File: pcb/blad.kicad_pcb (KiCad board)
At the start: 2 copper layers, 228.6 x 76.2 mm, 95 parts, among them J1 Conn_01x04, J2 Conn_01x02_Pin, SW1 1U, SW10 1U, SW11 1U, SW12 1U, SW13 1.25U, SW14 1U, SW15 1U, SW16 1U, SW17 1U, SW18 1U, SW19 1U, SW2 1U, SW20 1U, SW21 1U, SW22 1U, SW23 1.75U, SW24 1U, SW25 1U, SW26 1U, SW27 1U, SW28 1U, SW29 1U, SW3 1U, SW30 1U, SW31 1U, SW32 1U, SW33 1.25U, SW34 1.25U, SW35 1U, SW36 1.25U, SW37 2.75U, SW38 1.25U, SW39 1U, SW4 1U, SW40 1.25U, SW41 1.75U, SW42 2.25U, SW5 1U, SW6 1U, SW7 1U, SW8 1U, SW9 1U, U1 HY0020

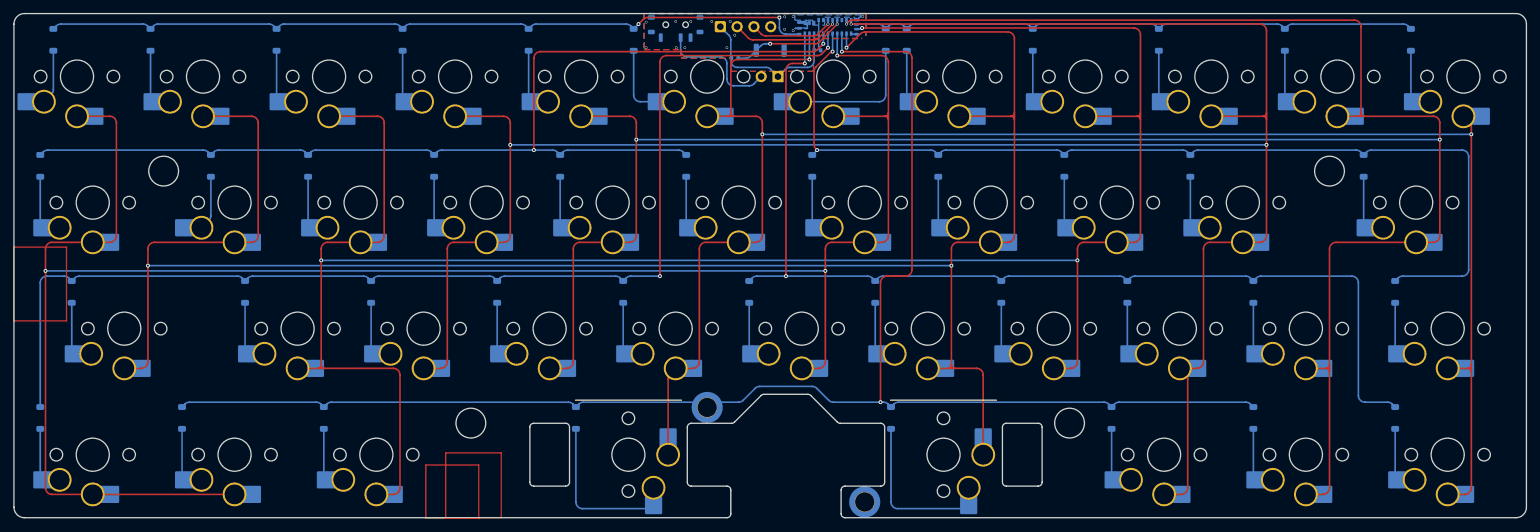
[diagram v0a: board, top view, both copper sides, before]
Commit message: Migrate PCB to MS88SF21 module
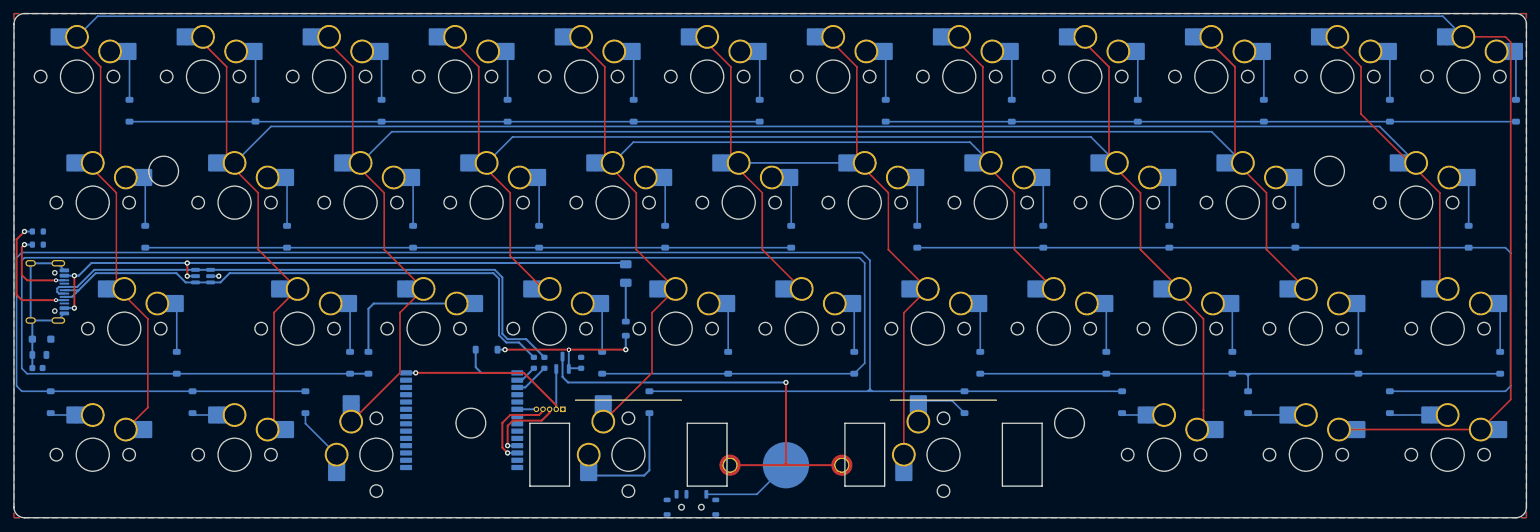
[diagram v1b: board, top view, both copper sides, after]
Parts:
- removed H1 (x2): MountingHole, Smidr:SMD-1_BD4.4-D2.8
- removed the SW25 at (151.6, 157.2)
- removed TS1: RST, Button_Switch_SMD:SW_Push_SPST_NO_Alps_SKRK
- added BT1: Battery_Cell, Smidr:BatteryHolder_Takachi_BS-S-1632, B.Cu at (206.4, 177.8)
- added D43: 1N5819W, Diode_SMD:D_SOD-123, B.Cu at (161.1, 160.3)
- added D44: SMF5.0CA, Diode_SMD:D_SOD-123F, B.Cu at (93.9, 158.8)
- added F1: PTC 500mA Hold, Fuse:Fuse_1206_3216Metric, B.Cu at (182.2, 148.8)
- added L1: BLM21PG121SN1D, Inductor_SMD:L_0805_2012Metric, B.Cu at (182.2, 157.2)
- added L2: BLM21PG121SN1D, Inductor_SMD:L_0805_2012Metric, B.Cu at (93.5, 161.1)
- added Q1: AO3401A, Package_TO_SOT_SMD:SOT-23, B.Cu at (172.6, 162.3)
- added R2: 100k, Resistor_SMD:R_0603_1608Metric, B.Cu at (175.4, 162.3)
- added R3: 5.1k, Resistor_SMD:R_0603_1608Metric, B.Cu at (93.3, 144.5)
- added R4: 27, Resistor_SMD:R_0603_1608Metric, B.Cu at (168.3, 162.3)
- added R5: 27, Resistor_SMD:R_0603_1608Metric, B.Cu at (169.9, 162.3)
- added SW26: 1U, Smidr:SW_Smidr_Choc_Hotswap, B.Cu at (151.6, 157.2)
- added U2: MS88SF21 1Y40AI-U, Smidr:RF_Module_MinewSemi_MS88SF21, B.Cu at (157.4, 174.1)
- C1: value 100nF -> 100n; footprint Capacitor_SMD:C_0402_1005Metric -> Capacitor_SMD:C_0603_1608Metric
- J1: value Conn_01x04 -> HRO_TYPE-C-31-M-12; footprint Connector_PinHeader_2.54mm:PinHeader_1x04_P2.54mm_Vertical -> Connector_USB:USB_C_Receptacle_HRO_TYPE-C-31-M-12
- J2: value Conn_01x02_Pin -> SWD; footprint Connector_PinHeader_2.54mm:PinHeader_1x02_P2.54mm_Vertical -> Connector_PinHeader_1.00mm:PinHeader_1x05_P1.00mm_Vertical
- R1: value 10k -> 5.1k; footprint Resistor_SMD:R_0402_1005Metric -> Resistor_SMD:R_0603_1608Metric
- U1: value HY0020 -> SRV05-4; footprint Smidr:RF_Module_FDK_HY0020 -> Package_TO_SOT_SMD:SOT-23-6
- moved C1 127.3 mm to (93.2, 163.1)
- moved J1 110.7 mm to (93.3, 151.6), turned to 90 degrees
- moved R1 108.5 mm to (93.3, 142.5)
- moved U1 101.7 mm to (118.3, 149.2), turned to 180 degrees
- moved S1 73.0 mm to (192.1, 184.2), turned to 180 degrees
- moved J2 59.9 mm to (172.7, 169.3)
- moved D6 21.9 mm to (202.4, 124.2), turned to 90 degrees
- moved D5 19.2 mm to (183.4, 124.2), turned to 90 degrees
- moved D8 19.2 mm to (240.5, 124.2), turned to 90 degrees
- moved D24 19.2 mm to (114.3, 162.3), turned to 90 degrees
- moved D34 19.2 mm to (314.3, 162.3), turned to 90 degrees
- moved D15 19.2 mm to (150.0, 143.3), turned to 90 degrees
- moved D20 19.2 mm to (245.3, 143.3), turned to 90 degrees
- moved D21 19.2 mm to (264.3, 143.3), turned to 90 degrees
- moved D28 19.2 mm to (197.6, 162.3), turned to 90 degrees
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- renumbered D41 to D24, D24 to D25, D25 to D26, D26 to D27, D27 to D28, D28 to D29, D29 to D30, D30 to D31, D31 to D32, D32 to D33, D33 to D34, D34 to D35, D35 to D36, D36 to D37, D37 to D38, D42 to D39, D38 to D40, D39 to D41, D40 to D42, SW41 to SW24, SW24 to SW25, SW26 to SW27, SW27 to SW28, SW28 to SW29, SW29 to SW30, SW30 to SW31, SW31 to SW32, SW32 to SW33, SW33 to SW34, SW34 to SW35, SW35 to SW36, SW36 to SW37, SW37 to SW38, SW42 to SW39, SW38 to SW40, SW39 to SW41, SW40 to SW42
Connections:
- C1 pad 1: +3V0 -> Earth
- D29 pad 1: ROW5 -> ROW4
- D34 pad 1: ROW3 -> ROW5
- D35 pad 1: ROW4 -> ROW6
- D35 pad 2: Net-(D34-A) (its old number) -> Net-(D35-A)
- D36 pad 2: Net-(D35-A) -> Net-(D36-A)
- D37 pad 2: Net-(D36-A) -> Net-(D37-A)
- D38 pad 2: Net-(D37-A) -> Net-(D38-A)
- D40 pad 2: Net-(D38-A) -> Net-(D40-A)
- D41 pad 1: ROW6 -> ROW5
- D41 pad 2: Net-(D39-A) (its old number) -> Net-(D41-A)
- D42 pad 1: ROW5 -> ROW3
- D42 pad 2: Net-(D40-A) -> Net-(D42-A)
- J2 pad 1: +3V0 -> GND
- J2 pad 2: Net-(J2-Pin_2) -> VDD
- R1 pad 1: +3V0 -> Net-(J1-CC1)
- R1 pad 2: nRESET -> GND
- S1 pad 1: unconnected-(S1-A-Pad1) -> Net-(BT1--)
- S1 pad 2: Net-(J2-Pin_2) -> GND
- S1 pad 3: GND -> unconnected-(S1-C-Pad3)
- SW10 pad 2: COL3 -> COL2
- SW11 pad 2: COL4 -> COL1
- SW12 pad 2: COL5 -> COL0
- SW19 pad 2: COL0 -> COL5
- SW20 pad 2: COL1 -> COL4
- SW21 pad 2: COL2 -> COL3
- SW22 pad 2: COL3 -> COL2
- SW23 pad 2: COL4 -> COL1
- SW24 pad 2: COL1 -> COL0
- SW25 pad 2: COL2 -> COL1
- SW27 pad 2: COL4 -> COL3
- SW28 pad 2: COL5 -> COL4
- SW29 pad 2: COL0 -> COL5
- SW30 pad 2: COL1 -> COL5
- SW31 pad 2: COL2 -> COL4
- SW33 pad 2: COL4 -> COL2
- SW34 pad 2: COL5 -> COL1
- SW35 pad 1: Net-(D34-A) (its old number) -> COL0
- SW35 pad 2: COL0 -> Net-(D35-A)
- SW36 pad 1: Net-(D35-A) -> COL1
- SW36 pad 2: COL0 -> Net-(D36-A)
- SW37 pad 1: Net-(D36-A) -> COL2
- SW37 pad 2: COL2 -> Net-(D37-A)
- SW38 pad 1: Net-(D37-A) -> COL4
- SW38 pad 2: COL5 -> Net-(D38-A)
- SW39 pad 2: COL1 -> COL5
- SW40 pad 1: Net-(D38-A) -> COL3
- SW40 pad 2: COL3 -> Net-(D40-A)
- SW41 pad 1: Net-(D39-A) (its old number) -> COL0
- SW41 pad 2: COL4 -> Net-(D41-A)
- SW42 pad 1: Net-(D40-A) -> COL0
- SW42 pad 2: COL5 -> Net-(D42-A)
- SW7 pad 2: COL0 -> COL5
- SW8 pad 2: COL1 -> COL4
- SW9 pad 2: COL2 -> COL3
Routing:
- net COL4: track 369.4 -> 172.0 mm, vias 3 -> 0
- net COL5: track 269.5 -> 133.3 mm, vias 3 -> 0
- net COL3: track 331.1 -> 209.8 mm, vias 3 -> 0
- net VBUS: track 0.00 -> 95.4 mm, vias 0 -> 4
- net USB_D+: track 0.00 -> 87.0 mm
- net USB_D-: track 0.00 -> 86.0 mm
- net ROW4: track 176.2 -> 252.4 mm, vias 2 -> 0
- net ROW5: track 157.3 -> 82.5 mm, vias 2 -> 0
- net COL2: track 323.0 -> 249.5 mm, vias 3 -> 0
- net COL0: track 297.8 -> 367.6 mm, vias 3 -> 0
- net +BATT: track 0.00 -> 67.7 mm, vias 0 -> 1
- net ROW2: track 160.0 -> 97.6 mm, vias 2 -> 0
- net ROW6: track 235.9 -> 285.7 mm, vias 2 -> 0
- net VDD: track 0.00 -> 31.4 mm, vias 0 -> 1
- net Earth: track 0.00 -> 27.2 mm
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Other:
- outline, holes or cut-outs redrawn

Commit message: Update PCB power wiring and stabilizer cutouts
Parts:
- moved L1 18.9 mm to (163.5, 154.4)
- moved F1 18.7 mm to (163.5, 148.8)
- moved D43 9.73 mm to (170.7, 162.3)
- moved R5 8.92 mm to (161.5, 159.1)
- moved R4 8.92 mm to (159.9, 159.1)
- moved Q1 4.27 mm to (170.6, 166.1), turned to 180 degrees
- moved D42 2.38 mm to (300.0, 168.3)
- moved D41 2.38 mm to (278.6, 168.3)
- moved R2 0.89 mm to (175.8, 163.1), turned to 90 degrees
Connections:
- SW39 pad 1: Net-(D39-A) -> COL5
- SW39 pad 2: COL5 -> Net-(D39-A)
- U2 pad 10: unconnected-(U2-P0.08-Pad10) -> ROW2
- U2 pad 11: unconnected-(U2-P1.09-Pad11) -> ROW5
- U2 pad 12: unconnected-(U2-P0.12-Pad12) -> COL3
- U2 pad 18: unconnected-(U2-P0.13-Pad18) -> ROW1
- U2 pad 19: unconnected-(U2-P0.15-Pad19) -> ROW3
- U2 pad 2: unconnected-(U2-P1.13-Pad2) -> COL0
- U2 pad 21: unconnected-(U2-P0.20-Pad21) -> COL4
- U2 pad 22: unconnected-(U2-P0.22-Pad22) -> COL5
- U2 pad 5: unconnected-(U2-P0.29-Pad5) -> COL1
- U2 pad 6: unconnected-(U2-P0.31-Pad6) -> COL2
- U2 pad 7: unconnected-(U2-P0.26-Pad7) -> ROW6
- U2 pad 8: unconnected-(U2-P0.04-Pad8) -> ROW4
- U2 pad 9: unconnected-(U2-P0.06-Pad9) -> ROW0
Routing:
- net ROW1: track 95.2 -> 289.9 mm, vias 0 -> 2
- net ROW3: track 128.7 -> 263.9 mm, vias 0 -> 2
- net ROW5: track 82.5 -> 171.9 mm, vias 0 -> 2
- net COL5: track 133.3 -> 213.9 mm, vias 0 -> 1
- net COL0: track 367.6 -> 422.6 mm
- net ROW0: track 95.2 -> 143.6 mm, vias 0 -> 2
- net COL3: track 209.8 -> 248.4 mm, vias 0 -> 1
- net COL1: track 295.9 -> 332.4 mm
- net ROW2: track 97.6 -> 123.5 mm, vias 0 -> 2
- net VBUS: track 95.4 -> 76.7 mm
- net ROW6: track 285.7 -> 302.3 mm, vias 0 -> 2
- net COL4: track 172.0 -> 185.3 mm
- net ROW4: track 252.4 -> 263.2 mm, vias 0 -> 2
- net Net-(D39-A): track 7.74 -> 18.2 mm
- net USB_D+: track 87.0 -> 77.5 mm
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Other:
- outline, holes or cut-outs redrawn

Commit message: Add logo footprint to PCB
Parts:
- added G***: LOGO, Smidr:logo, F.Cu at (204.0, 147.6)
- moved U1 3.57 mm to (121.8, 149.2)
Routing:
- net ROW4: track 263.2 -> 223.0 mm, vias 2 -> 0
- net ROW6: track 302.3 -> 269.0 mm
- net GND: vias 1677 -> 1661
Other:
- outline, holes or cut-outs redrawn

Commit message: Fix USB grounding and add battery bulk capacitor
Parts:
- removed D44: SMF5.0CA, Diode_SMD:D_SOD-123F
- C1: value 100n -> 100u; footprint Capacitor_SMD:C_0603_1608Metric -> Capacitor_SMD:C_1206_3216Metric
- moved C1 96.6 mm to (189.7, 169.1), turned to -90 degrees
- moved L2 2.39 mm to (93.3, 158.8)
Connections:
- C1 pad 1: Earth -> +BATT
- J1 pad A1: Earth -> GND
- J1 pad A12: Earth -> GND
- J1 pad B1: Earth -> GND
- J1 pad B12: Earth -> GND
- J1 pad SH: Earth -> Net-(J1-SHIELD)
- L2 pad 2: Earth -> Net-(J1-SHIELD)
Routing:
- net Earth: track 27.2 -> 0.00 mm
- net Net-(J1-SHIELD): track 0.00 -> 19.8 mm
- net GND: vias 1661 -> 1669
